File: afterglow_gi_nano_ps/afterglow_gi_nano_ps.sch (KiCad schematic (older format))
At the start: 64 parts, among them J1 Conn_02x17_Odd_Even, J2 POWER_CONN, J3 GI_WPC_J120, J4 GI_WPC_J121, J5 GI_CONN_J119, J6 Conn_01x12_Male, Q1 FQP30N06L, Q2 FQP30N06L, Q3 FQP30N06L, Q4 FQP30N06L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

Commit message: A PCB layout proposal
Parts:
- J6: footprint Connectors_Molex:Molex_KK-6410-12_12x2.54mm_Straight -> Connectors_Molex:Molex_KK-41791-12_10x3.96mm_Straight
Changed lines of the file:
@@
 F 0 "J6" H 6008 1981 50  0000 C CNN
 F 1 "Conn_01x12_Male" H 6008 1890 50  0000 C CNN
-F 2 "Connectors_Molex:Molex_KK-6410-12_12x2.54mm_Straight" H 5900 1300 50  0001 C CNN
+F 2 "Connectors_Molex:Molex_KK-41791-12_10x3.96mm_Straight" H 5900 1300 50  0001 C CNN
 F 3 "~" H 5900 1300 50  0001 C CNN
 	1    5900 1300

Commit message: Some progress
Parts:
- Q6, Q7, Q8, Q9: footprint digikey-footprints:TO-220-3 -> TO_SOT_Packages_THT:TO-220_Vertical
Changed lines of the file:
@@
 F 0 "Q7" H 7408 2353 60  0000 L CNN
 F 1 "FQP30N06L" H 7408 2247 60  0000 L CNN
-F 2 "digikey-footprints:TO-220-3" H 7500 2500 60  0001 L CNN
+F 2 "TO_SOT_Packages_THT:TO-220_Vertical" H 7500 2500 60  0001 L CNN
 F 3 "https://www.fairchildsemi.com/datasheets/FQ/FQP30N06L.pdf" H 7500 2600 60  0001 L CNN
 F 4 "FQP30N06L-ND" H 7500 2700 60  0001 L CNN "Digi-Key_PN"
@@
 F 0 "Q9" H 9258 2353 60  0000 L CNN
 F 1 "FQP30N06L" H 9258 2247 60  0000 L CNN
-F 2 "digikey-footprints:TO-220-3" H 9350 2500 60  0001 L CNN
+F 2 "TO_SOT_Packages_THT:TO-220_Vertical" H 9350 2500 60  0001 L CNN
 F 3 "https://www.fairchildsemi.com/datasheets/FQ/FQP30N06L.pdf" H 9350 2600 60  0001 L CNN
 F 4 "FQP30N06L-ND" H 9350 2700 60  0001 L CNN "Digi-Key_PN"
@@
 F 0 "Q8" H 9258 1503 60  0000 L CNN
 F 1 "FQP30N06L" H 9258 1397 60  0000 L CNN
-F 2 "digikey-footprints:TO-220-3" H 9350 1650 60  0001 L CNN
+F 2 "TO_SOT_Packages_THT:TO-220_Vertical" H 9350 1650 60  0001 L CNN
 F 3 "https://www.fairchildsemi.com/datasheets/FQ/FQP30N06L.pdf" H 9350 1750 60  0001 L CNN
 F 4 "FQP30N06L-ND" H 9350 1850 60  0001 L CNN "Digi-Key_PN"
@@
 F 0 "Q6" H 7058 1853 60  0000 L CNN
 F 1 "FQP30N06L" H 7058 1747 60  0000 L CNN
-F 2 "digikey-footprints:TO-220-3" H 7150 2000 60  0001 L CNN
+F 2 "TO_SOT_Packages_THT:TO-220_Vertical" H 7150 2000 60  0001 L CNN
 F 3 "https://www.fairchildsemi.com/datasheets/FQ/FQP30N06L.pdf" H 7150 2100 60  0001 L CNN
 F 4 "FQP30N06L-ND" H 7150 2200 60  0001 L CNN "Digi-Key_PN"

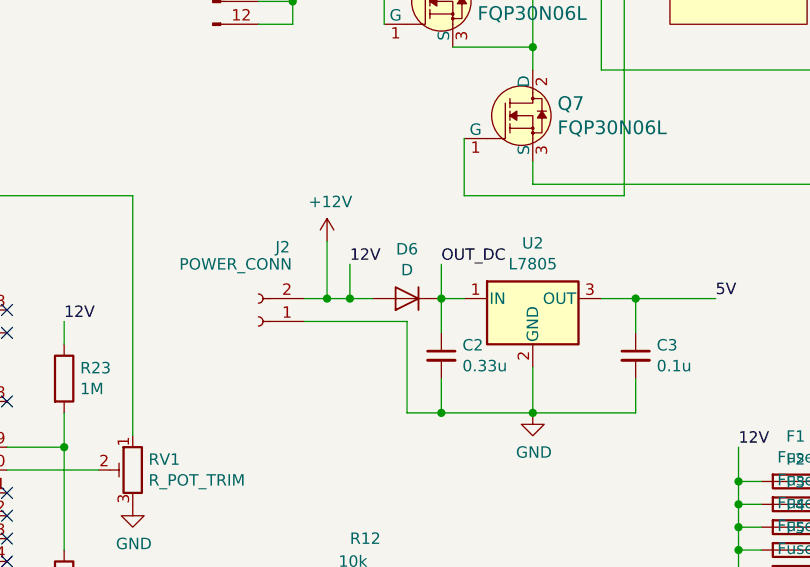
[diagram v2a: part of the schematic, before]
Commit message: New PCB layout with power supply
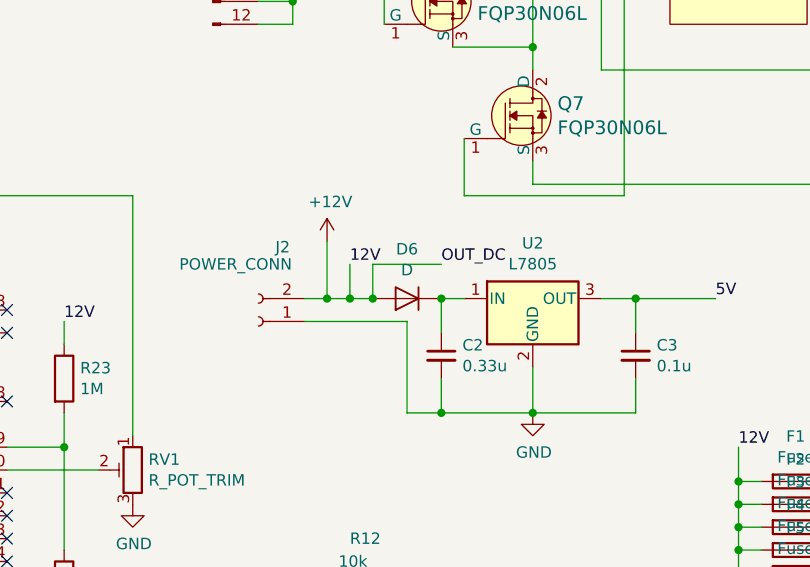
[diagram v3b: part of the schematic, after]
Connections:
- net +12V: now also C4.1, C5.1, C6.1, C7.1, C8.1, Q6.2 (D), Q8.2 (D), U3.6 (OUTP)
- removed net OUT_DC: C2.1, C4.1, C5.1, C6.1, C7.1, C8.1, D6.1 (K), Q6.2 (D), Q8.2 (D), U2.1 (IN), U3.6 (OUTP)
- new net: C2.1, D6.1 (K), U2.1 (IN)
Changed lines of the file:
@@
 Wire Wire Line
 	9500 1050 9700 1050
-Wire Wire Line
-	6900 3100 6900 2950
 Text Label 6900 2950 0    50   ~ 0
 OUT_DC
@@
 Wire Wire Line
 	6750 1000 8800 1000
+Wire Wire Line
+	6600 3100 6600 2950
+Wire Wire Line
+	6600 2950 6900 2950
+Connection ~ 6600 3100
 $EndSCHEMATC
